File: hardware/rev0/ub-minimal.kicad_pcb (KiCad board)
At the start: 4 copper layers, 38 x 16 mm, 67 parts, among them P1 ANT, P2 CONN_01X06, U1 WT325BI0032.000000, U2 SX1276, U3 M10478, U4 STM32F048GUx, U5 CAT24M01, U6 MS5637, U7 LD3985G30R, U8 LM3671

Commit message: Replace TCXO with XTAL
Planned TCXO became obsolete and hard to source, high quality XTAL
should be good enough with possible temperature compensation in
software.
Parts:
- removed C29: 10n, Capacitors_SMD:C_0603
- removed C30: 1u, Capacitors_SMD:C_0603
- removed L1: FERRITE, Resistors_SMD:R_0603
- removed R13: 10k, Resistors_SMD:R_0402
- removed U1: WT325BI0032.000000, Custom Parts:TCXO-WT325
- removed U7: LD3985G30R, Housings_SOT-23_SOT-143_TSOT-6:SOT-23-5
- added X1: 32M, Custom Parts:XTAL-2x2.5, B.Cu at (78.5, 54.5)
- C1: value 100n -> 10p
- C3: value 10n -> 10p
- moved C3 3.54 mm to (76.0, 54.5), turned to 270 degrees
- moved C1 2.85 mm to (78.8, 56.5), turned to 180 degrees
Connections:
- C3 pad 2: /MCU/OSCIN -> GND
- U2 pad 10: Net-(U2-Pad10) -> (no net)
- U2 pad 11: Net-(U2-Pad11) -> (no net)
- U2 pad 12: Net-(U2-Pad12) -> (no net)
- U2 pad 20: Net-(U2-Pad20) -> (no net)
- U2 pad 21: Net-(U2-Pad21) -> (no net)
- U2 pad 22: Net-(U2-Pad22) -> (no net)
- U2 pad 27: Net-(U2-Pad27) -> (no net)
- U2 pad 5: Net-(C3-Pad1) -> Net-(C1-Pad1)
- U2 pad 6: Net-(U2-Pad6) -> Net-(C3-Pad1)
- U2 pad 9: Net-(U2-Pad9) -> (no net)
- U3 pad 10: Net-(U3-Pad10) -> (no net)
- U3 pad 11: Net-(U3-Pad11) -> (no net)
- U3 pad 12: Net-(U3-Pad12) -> (no net)
- U3 pad 16: Net-(U3-Pad16) -> (no net)
- U3 pad 17: Net-(U3-Pad17) -> (no net)
- U3 pad 23: Net-(U3-Pad23) -> (no net)
- U4 pad 19: Net-(U4-Pad19) -> (no net)
- U4 pad 2: Net-(C29-Pad1) -> (no net)
- U4 pad 20: Net-(U4-Pad20) -> (no net)
- U4 pad 23: Net-(U4-Pad23) -> (no net)
- U4 pad 24: Net-(U4-Pad24) -> (no net)
- U4 pad 25: Net-(U4-Pad25) -> (no net)
- U4 pad 26: Net-(U4-Pad26) -> (no net)
- U4 pad 3: Net-(R13-Pad2) -> (no net)
- U5 pad 1: Net-(U5-Pad1) -> (no net)
- U5 pad 7: Net-(U5-Pad7) -> (no net)
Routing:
- net 3V0: track 65.6 -> 0.00 mm, vias 2 -> 0
- net Net-(C29-Pad1): track 15.2 -> 0.00 mm
- net /MCU/OSCIN: track 9.19 -> 0.00 mm
- net GND: track 224.3 -> 231.6 mm, vias 94 -> 97
- net +BATT: track 17.9 -> 12.4 mm
- net Net-(C1-Pad1): track 3.33 -> 8.83 mm, vias 0 -> 1
- net Net-(C3-Pad1): track 2.38 -> 4.56 mm
- net Net-(R13-Pad2): track 2.14 -> 0.00 mm

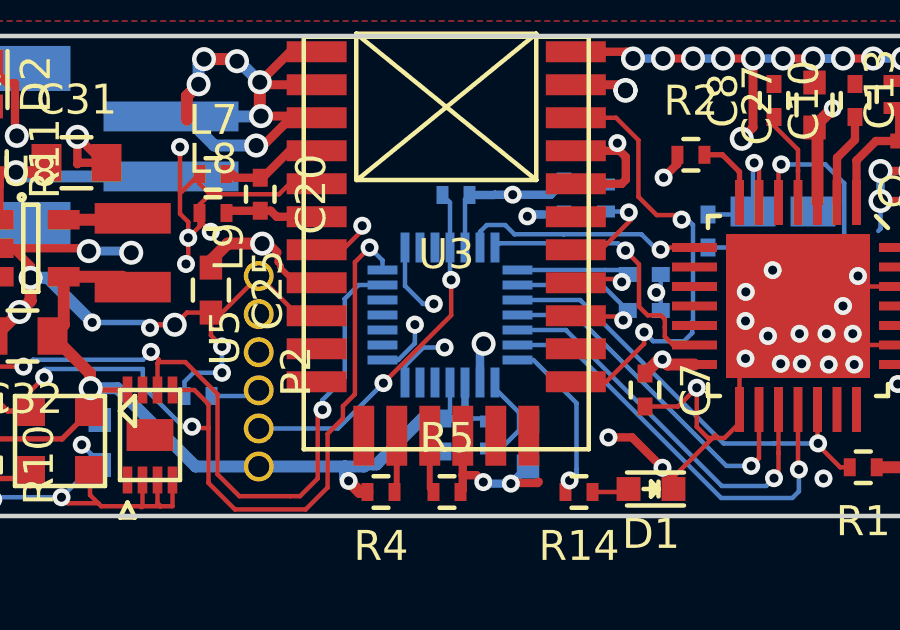
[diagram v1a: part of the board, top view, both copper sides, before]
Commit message: DRC alterations, generate gerbers
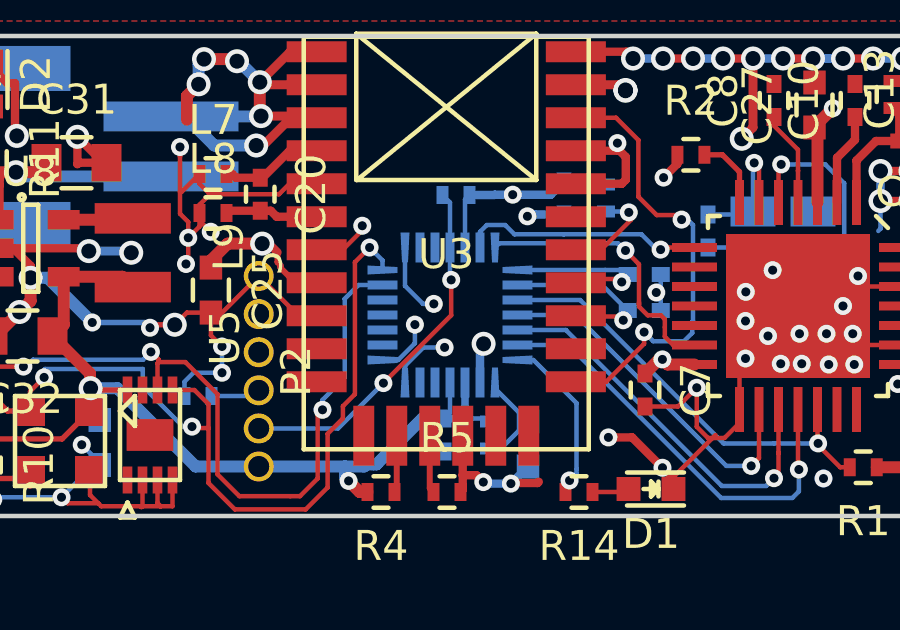
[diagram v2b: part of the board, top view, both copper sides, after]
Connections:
- U2 pad 10: (no net) -> Net-(U2-Pad10)
- U2 pad 11: (no net) -> Net-(U2-Pad11)
- U2 pad 12: (no net) -> Net-(U2-Pad12)
- U2 pad 20: (no net) -> Net-(U2-Pad20)
- U2 pad 21: (no net) -> Net-(U2-Pad21)
- U2 pad 22: (no net) -> Net-(U2-Pad22)
- U2 pad 27: (no net) -> Net-(U2-Pad27)
- U2 pad 9: (no net) -> Net-(U2-Pad9)
- U3 pad 10: (no net) -> Net-(U3-Pad10)
- U3 pad 11: (no net) -> Net-(U3-Pad11)
- U3 pad 12: (no net) -> Net-(U3-Pad12)
- U3 pad 16: (no net) -> Net-(U3-Pad16)
- U3 pad 17: (no net) -> Net-(U3-Pad17)
- U3 pad 23: (no net) -> Net-(U3-Pad23)
- U4 pad 19: (no net) -> Net-(U4-Pad19)
- U4 pad 2: (no net) -> Net-(U4-Pad2)
- U4 pad 20: (no net) -> Net-(U4-Pad20)
- U4 pad 23: (no net) -> Net-(U4-Pad23)
- U4 pad 24: (no net) -> Net-(U4-Pad24)
- U4 pad 25: (no net) -> Net-(U4-Pad25)
- U4 pad 26: (no net) -> Net-(U4-Pad26)
- U4 pad 3: (no net) -> Net-(U4-Pad3)
- U5 pad 1: (no net) -> Net-(U5-Pad1)
- U5 pad 7: (no net) -> Net-(U5-Pad7)

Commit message: Various fixes and tweaks
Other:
- board text added: "+441234567890"
- board text added: "B0"
- board text added: "CK"
- board text added: "DAT"
- board text added: "DS0.ME"
- board text added: "GND"
- board text added: "RST"
- board text added: "UBr0"
- board text added: "V+"
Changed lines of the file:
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@@
     (links 155)
     (no_connects 0)
-    (area 40 40 102.500001 82.500001)
+    (area 50.924999 47.924999 89.075001 64.075001)
     (thickness 1)
-    (drawings 5)
+    (drawings 18)
     (tracks 881)
     (zones 0)
@@
     (0 F.Cu signal)
     (1 In1.Cu signal hide)
-    (2 In2.Cu signal hide)
+    (2 In2.Cu signal)
     (31 B.Cu signal)
     (32 B.Adhes user)
@@
     (visible_elements 7FFCFFFF)
     (pcbplotparams
-      (layerselection 0x00000_00000006)
+      (layerselection 0x010f0_80000007)
       (usegerberextensions true)
       (excludeedgelayer true)
@@
       (net 31 "/LORA TX/ANT"))
   )
-  (module "Custom Parts:6-1.27mm" (layer F.Cu)
-    (at 61.025 59.175 90)
-    (fp_text reference P2 (at 0 1.25 90) (layer F.SilkS)
-      (effects (font (size 1 1) (thickness 0.15)))
-    )
-    (fp_text value CONN_01X06 (at 0 -1.27 90) (layer F.Fab)
-      (effects (font (size 1 1) (thickness 0.15)))
-    )
-    (pad 1 thru_hole circle (at -3.175 0 90) (size 1 1) (drill 0.7) (layers *.Cu *.Mask F.SilkS)
-      (net 2 +1V8))
-    (pad 2 thru_hole circle (at -1.905 0 90) (size 1 1) (drill 0.7) (layers *.Cu *.Mask F.SilkS)
-      (net 7 "Net-(P2-Pad2)"))
-    (pad 3 thru_hole circle (at -0.635 0 90) (size 1 1) (drill 0.7) (layers *.Cu *.Mask F.SilkS)
-      (net 8 "Net-(P2-Pad3)"))
-    (pad 4 thru_hole circle (at 0.635 0 90) (size 1 1) (drill 0.7) (layers *.Cu *.Mask F.SilkS)
-      (net 12 "Net-(P2-Pad4)"))
-    (pad 5 thru_hole circle (at 1.905 0 90) (size 1 1) (drill 0.7) (layers *.Cu *.Mask F.SilkS)
-      (net 13 "Net-(P2-Pad5)"))
-    (pad 6 thru_hole circle (at 3.175 0 90) (size 1 1) (drill 0.7) (layers *.Cu *.Mask F.SilkS)
-      (net 1 GND))
-  )
   (module Resistors_SMD:R_0402 (layer F.Cu)
     (at 81.175 62.375 180)
@@
       (net 10 /MCU/I2C_SDA))
   )
+  (module "Custom Parts:6-1.27mm" (layer F.Cu)
+    (at 61.025 59.175 90)
+    (fp_text reference P2 (at 0 1.25 90) (layer F.SilkS)
+      (effects (font (size 1 1) (thickness 0.15)))
+    )
+    (fp_text value CONN_01X06 (at 0 -1.27 90) (layer F.Fab)
+      (effects (font (size 1 1) (thickness 0.15)))
+    )
+    (pad 1 thru_hole circle (at -3.175 0 90) (size 1 1) (drill 0.7) (layers *.Cu *.Mask F.SilkS)
+      (net 2 +1V8))
+    (pad 2 thru_hole circle (at -1.905 0.0635 90) (size 1 1) (drill 0.7) (layers *.Cu *.Mask F.SilkS)
+      (net 7 "Net-(P2-Pad2)"))
+    (pad 3 thru_hole circle (at -0.635 -0.0635 90) (size 1 1) (drill 0.7) (layers *.Cu *.Mask F.SilkS)
+      (net 8 "Net-(P2-Pad3)"))
+    (pad 4 thru_hole circle (at 0.635 -0.0635 90) (size 1 1) (drill 0.7) (layers *.Cu *.Mask F.SilkS)
+      (net 12 "Net-(P2-Pad4)"))
+    (pad 5 thru_hole circle (at 1.905 0.0635 90) (size 1 1) (drill 0.7) (layers *.Cu *.Mask F.SilkS)
+      (net 13 "Net-(P2-Pad5)"))
+    (pad 6 thru_hole circle (at 3.175 0 90) (size 1 1) (drill 0.7) (layers *.Cu *.Mask F.SilkS)
+      (net 1 GND))
+  )
+  (gr_text +441234567890 (at 79.3 63) (layer B.SilkS)
+    (effects (font (size 1.2 1.2) (thickness 0.22)) (justify mirror))
+  )
+  (gr_text V+ (at 61.5 62.6) (layer B.SilkS)
+    (effects (font (size 1 1) (thickness 0.2)) (justify right mirror))
+  )
+  (gr_text RST (at 61.7 61.3) (layer B.SilkS)
+    (effects (font (size 1 1) (thickness 0.2)) (justify right mirror))
+  )
+  (gr_text B0 (at 61.7 60) (layer B.SilkS)
+    (effects (font (size 1 1) (thickness 0.2)) (justify right mirror))
+  )
+  (gr_text DAT (at 61.6 58.7) (layer B.SilkS)
+    (effects (font (size 1 1) (thickness 0.2)) (justify right mirror))
+  )
+  (gr_text CK (at 61.6 57.4) (layer B.SilkS)
+    (effects (font (size 1 1) (thickness 0.2)) (justify right mirror))
+  )
+  (gr_text GND (at 61.6 56.1) (layer B.SilkS)
+    (effects (font (size 1 1) (thickness 0.2)) (justify right mirror))
+  )
+  (gr_line (start 59.9 54.2) (end 60 54.2) (angle 90) (layer B.SilkS) (width 0.2))
+  (gr_line (start 59.9 53.5) (end 59.9 54.2) (angle 90) (layer B.SilkS) (width 0.2))
+  (gr_line (start 59.5 53.9) (end 60.4 53.9) (angle 90) (layer B.SilkS) (width 0.2))
+  (gr_line (start 59.6 49.7) (end 60.4 49.7) (angle 90) (layer B.SilkS) (width 0.2))
+  (gr_text UBr0 (at 67 51.5) (layer B.SilkS)
+    (effects (font (size 1.5 1.5) (thickness 0.3)) (justify mirror))
+  )
+  (gr_text DS0.ME (at 67 49.5) (layer B.SilkS)
+    (effects (font (size 1.5 1.5) (thickness 0.3)) (justify mirror))
+  )
   (gr_line (start 89 48) (end 89 64) (angle 90) (layer Edge.Cuts) (width 0.15))

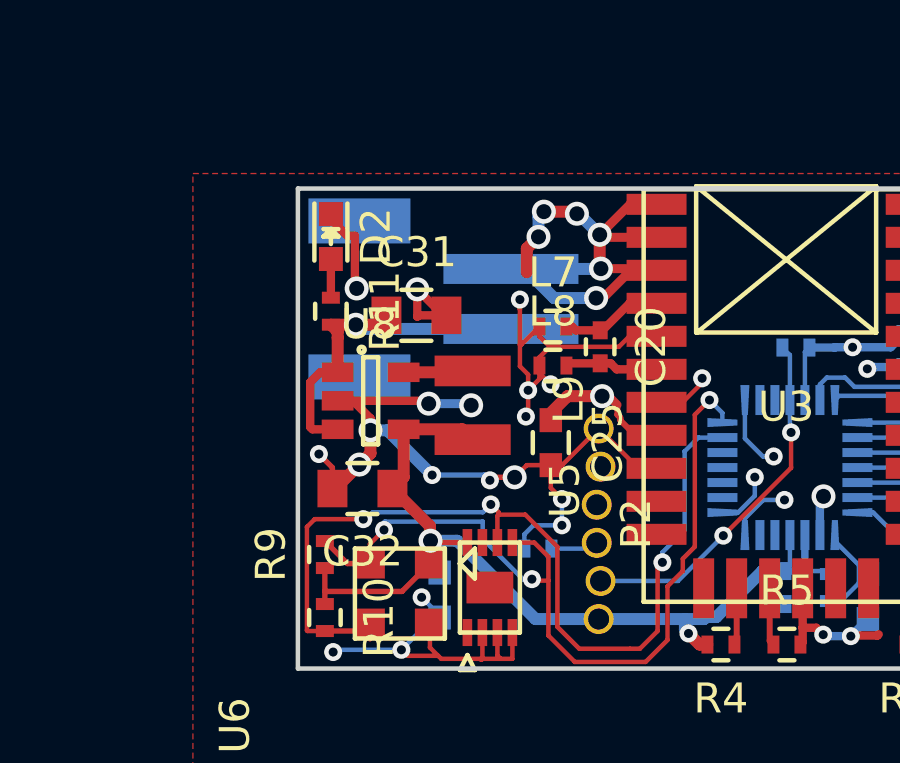
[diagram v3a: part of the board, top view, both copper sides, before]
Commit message: Add FB network
Allow system to run off 2V if needed
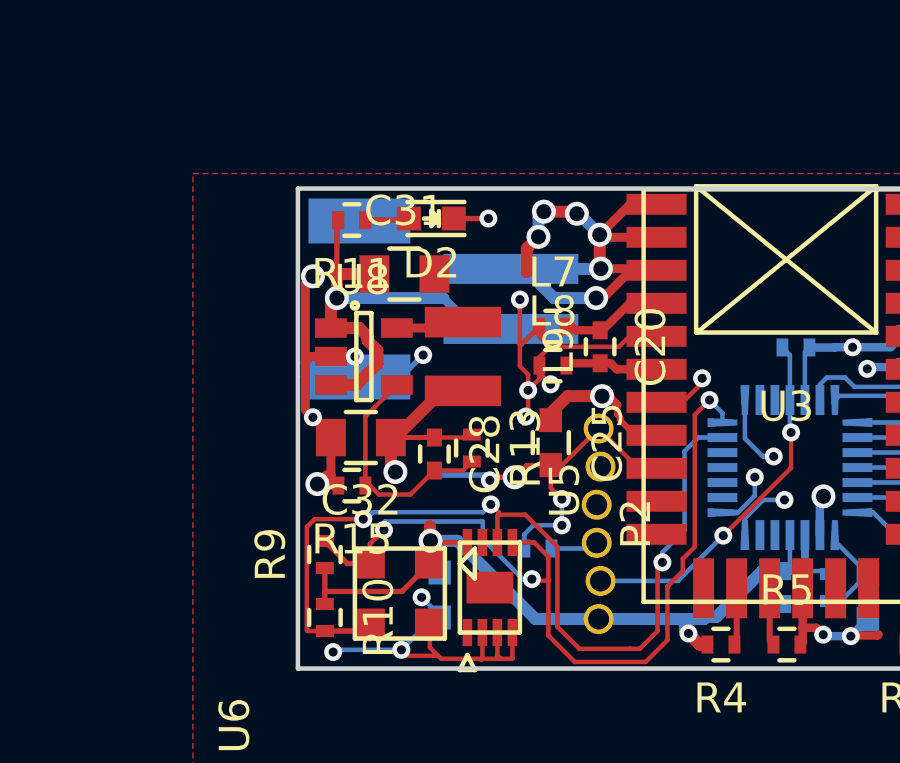
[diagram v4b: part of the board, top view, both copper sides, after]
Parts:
- added C28: 8.2p, Capacitors_SMD:C_0402, F.Cu at (55.5, 56.9)
- added R13: 300k, Resistors_SMD:R_0402, F.Cu at (56.8, 56.6)
- added R15: 100k, Resistors_SMD:R_0402, F.Cu at (52.8, 57.9)
- moved D2 3.40 mm to (55.5, 49.0), turned to 180 degrees
- moved R11 3.12 mm to (52.8, 49.0), turned to 180 degrees
- moved C32 1.70 mm to (53.1, 56.3)
- moved L9 1.66 mm to (56.5, 53.6)
- moved U8 1.49 mm to (53.2, 53.6)
- moved C31 1.43 mm to (54.5, 50.9)
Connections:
- BT1 pad : (no net) -> GND
- U2 pad 10: Net-(U2-Pad10) -> (no net)
- U2 pad 11: Net-(U2-Pad11) -> (no net)
- U2 pad 12: Net-(U2-Pad12) -> (no net)
- U2 pad 20: Net-(U2-Pad20) -> (no net)
- U2 pad 21: Net-(U2-Pad21) -> (no net)
- U2 pad 22: Net-(U2-Pad22) -> (no net)
- U2 pad 27: Net-(U2-Pad27) -> (no net)
- U2 pad 9: Net-(U2-Pad9) -> (no net)
- U3 pad 10: Net-(U3-Pad10) -> (no net)
- U3 pad 11: Net-(U3-Pad11) -> (no net)
- U3 pad 12: Net-(U3-Pad12) -> (no net)
- U3 pad 16: Net-(U3-Pad16) -> (no net)
- U3 pad 17: Net-(U3-Pad17) -> (no net)
- U3 pad 23: Net-(U3-Pad23) -> (no net)
- U4 pad 19: Net-(U4-Pad19) -> (no net)
- U4 pad 2: Net-(U4-Pad2) -> (no net)
- U4 pad 20: Net-(U4-Pad20) -> (no net)
- U4 pad 23: Net-(U4-Pad23) -> (no net)
- U4 pad 24: Net-(U4-Pad24) -> (no net)
- U4 pad 25: Net-(U4-Pad25) -> (no net)
- U4 pad 26: Net-(U4-Pad26) -> (no net)
- U4 pad 3: Net-(U4-Pad3) -> (no net)
- U5 pad 1: Net-(U5-Pad1) -> (no net)
- U5 pad 7: Net-(U5-Pad7) -> (no net)
- U8 pad 4: +1V8 -> Net-(C28-Pad2)
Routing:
- net Net-(C28-Pad2): track 0.00 -> 7.91 mm
- net +1V8: track 124.9 -> 130.7 mm, vias 9 -> 10
- net GND: track 231.6 -> 226.4 mm, vias 97 -> 95
- net +BATT: track 12.4 -> 15.4 mm
